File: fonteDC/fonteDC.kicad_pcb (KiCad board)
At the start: 2 copper layers, 13 parts, among them U1 LM7805_TO220

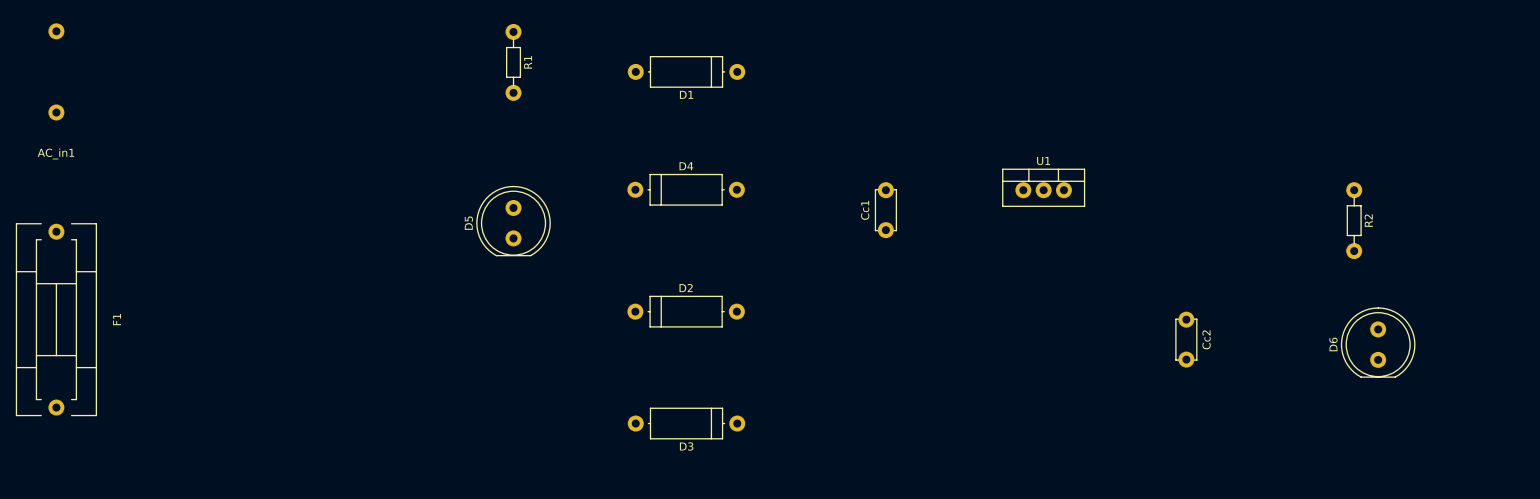
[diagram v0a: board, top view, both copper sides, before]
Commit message: Adicionando capacitores e porta fusível
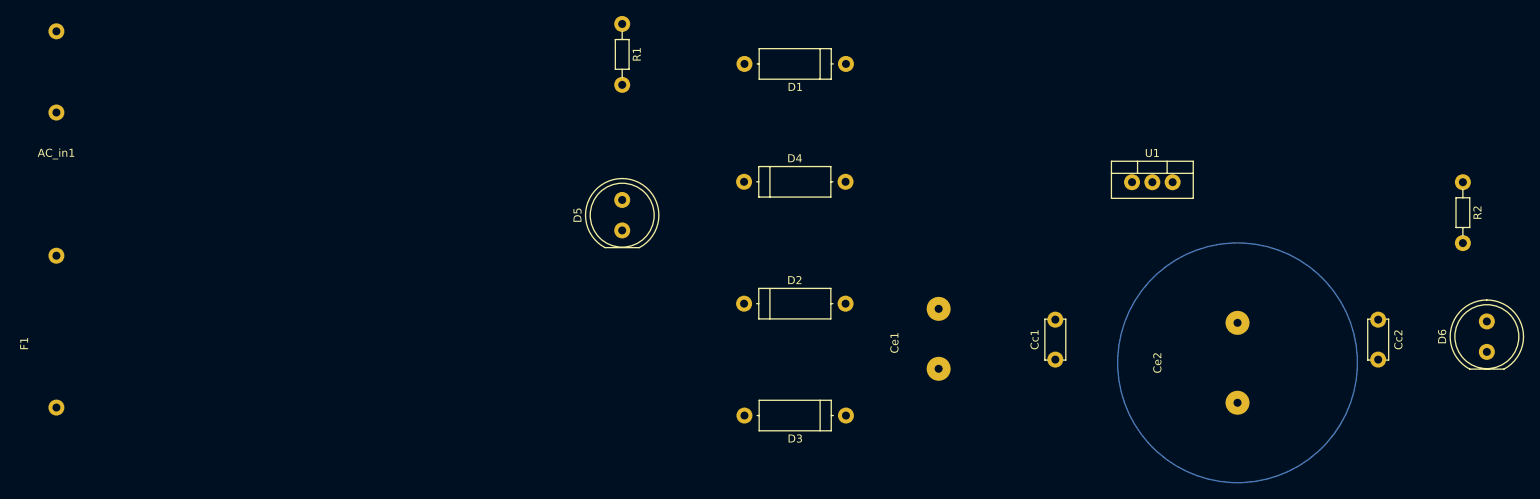
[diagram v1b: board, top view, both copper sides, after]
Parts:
- added Ce1: CP1, fonteDC:CP_elet_7mF, F.Cu at (150.2, 69.4)
- added Ce2: CP1, fonteDC:CP_elet_10mF, F.Cu at (187.6, 66.4)
- F1: footprint fonteDC:Fuseholder5x20_horiz_SemiClosed_Casing10x25mm -> fonteDC:fuseholder
- moved Cc1 26.7 mm to (164.8, 81.0)
- moved Cc2 24.0 mm to (205.2, 76.0)
- moved D6 13.6 mm to (218.8, 79.4)
- moved R2 13.6 mm to (215.8, 58.8)
- moved D1 13.6 mm to (138.6, 44.0)
- moved D2 13.6 mm to (125.8, 74.0)
- moved D3 13.6 mm to (138.6, 88.0)
- moved D4 13.6 mm to (125.8, 58.8)
- moved D5 13.6 mm to (110.6, 64.2)
- moved R1 13.6 mm to (110.6, 39.0)
- moved U1 13.6 mm to (174.4, 58.8)

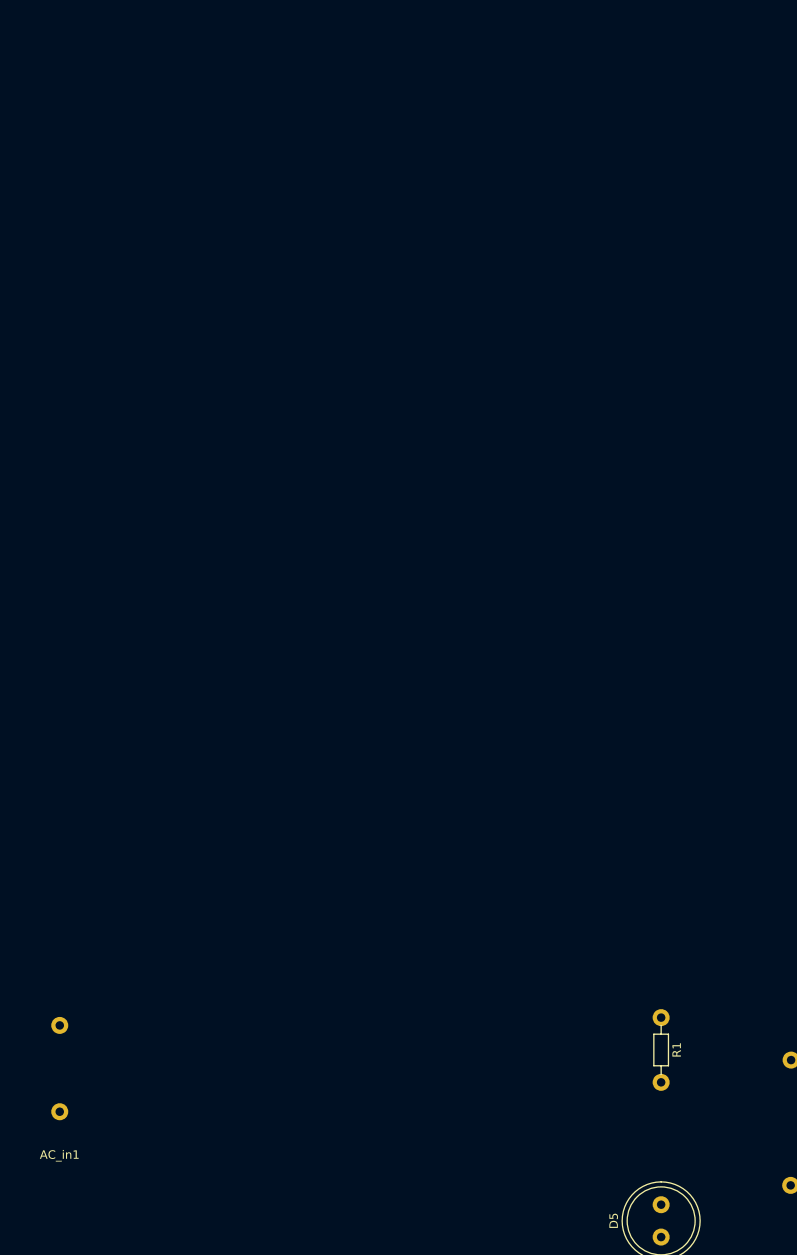
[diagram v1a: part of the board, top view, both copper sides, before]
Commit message: Adicionando footprints da chave seletora de tensão e do transformador
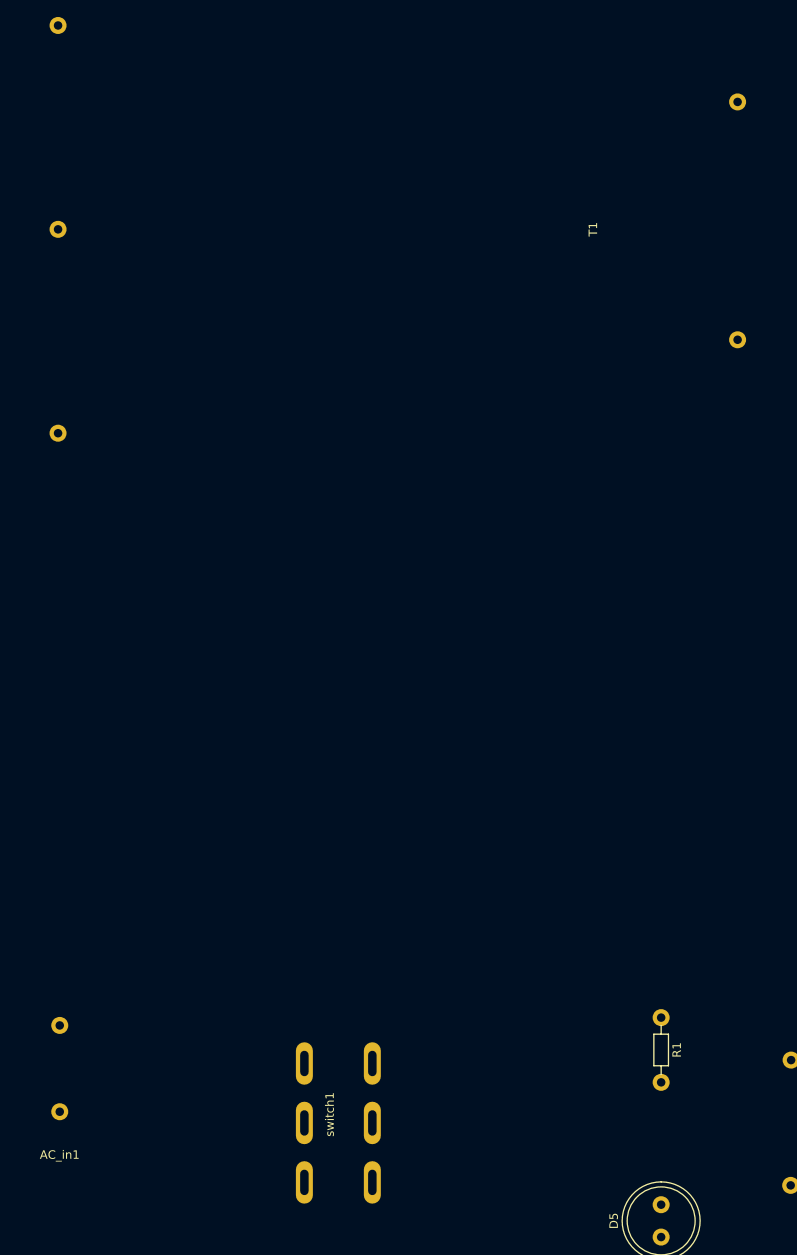
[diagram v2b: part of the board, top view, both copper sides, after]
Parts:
- added T1: Transformer_1P_SS, fonteDC:transformer, F.Cu at (79.6, -9.80)
- added switch1: voltage_switch, fonteDC:swich_110_220, F.Cu at (72.6, 36.4)
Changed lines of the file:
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@@
 (kicad_pcb (version 4) (host pcbnew 4.0.7)
   (general
-    (links 23)
-    (no_connects 23)
+    (links 32)
+    (no_connects 32)
     (area 0 0 0 0)
     (thickness 1.6)
@@
     (tracks 1)
     (zones 0)
-    (modules 15)
-    (nets 9)
+    (modules 17)
+    (nets 11)
   )
   (page A4)
@@
   (net 7 "Net-(AC_in1-Pad2)")
   (net 8 "Net-(AC_in1-Pad1)")
+  (net 9 "Net-(T1-Pad4)")
+  (net 10 "Net-(T1-Pad3)")
   (net_class Default "This is the default net class."
     (clearance 0.2)
@@
     (add_net "Net-(D5-Pad2)")
     (add_net "Net-(D6-Pad2)")
+    (add_net "Net-(T1-Pad3)")
+    (add_net "Net-(T1-Pad4)")
   )
   (module fonteDC:AC_in (layer F.Cu)
@@
       (net 1 GND))
   )
+  (module fonteDC:swich_110_220 (layer F.Cu)
+    (at 72.6 36.4 270)
+    (fp_text reference switch1 (at 14 1 270) (layer F.SilkS)
+      (effects (font (size 1 1) (thickness 0.15)))
+    )
+    (fp_text value voltage_switch (at 14 -2 270) (layer F.Fab)
+      (effects (font (size 1 1) (thickness 0.15)))
+    )
+    (fp_text user VDD110 (at 24 7 270) (layer F.Fab)
+      (effects (font (size 1 1) (thickness 0.15)))
+    )
+    (fp_text user GND110 (at 24 -7 270) (layer F.Fab)
+      (effects (font (size 1 1) (thickness 0.15)))
+    )
+    (fp_text user GND220 (at 6 -7 270) (layer F.Fab)
+      (effects (font (size 1 1) (thickness 0.15)))
+    )
+    (fp_text user VDD220 (at 6 7 270) (layer F.Fab)
+      (effects (font (size 1 1) (thickness 0.15)))
+    )
+    (fp_text user GND (at 15 -7 270) (layer F.Fab)
+      (effects (font (size 1 1) (thickness 0.15)))
+    )
+    (fp_text user VDD (at 15 7 270) (layer F.Fab)
+      (effects (font (size 1 1) (thickness 0.15)))
+    )
+    (fp_line (start 0 -8) (end 0 8) (layer F.Fab) (width 0.15))
+    (fp_line (start 30 -8) (end 30 8) (layer F.Fab) (width 0.15))
+    (fp_line (start 0 8) (end 30 8) (layer F.Fab) (width 0.15))
+    (fp_line (start 0 -8) (end 30 -8) (layer F.Fab) (width 0.15))
+    (pad 6 thru_hole oval (at 22 -4 270) (size 5 2) (drill oval 3 1) (layers *.Cu *.Mask)
+      (net 1 GND))
+    (pad 5 thru_hole oval (at 22 4 270) (size 5 2) (drill oval 3 1) (layers *.Cu *.Mask)
+      (net 9 "Net-(T1-Pad4)"))
+    (pad 4 thru_hole oval (at 8 -4 270) (size 5 2) (drill oval 3 1) (layers *.Cu *.Mask)
+      (net 1 GND))
+    (pad 3 thru_hole oval (at 8 4 270) (size 5 2) (drill oval 3 1) (layers *.Cu *.Mask)
+      (net 10 "Net-(T1-Pad3)"))
+    (pad 2 thru_hole oval (at 15 -4 270) (size 5 2) (drill oval 3 1) (layers *.Cu *.Mask)
+      (net 1 GND))
+    (pad 1 thru_hole oval (at 15 4 270) (size 5 2) (drill oval 3 1) (layers *.Cu *.Mask)
+      (net 8 "Net-(AC_in1-Pad1)"))
+  )
+  (module fonteDC:transformer (layer F.Cu)
+    (at 79.6 -9.8 90)
+    (fp_text reference T1 (at 44 23 90) (layer F.SilkS)
+      (effects (font (size 1 1) (thickness 0.15)))
+    )
+    (fp_text value Transformer_1P_SS (at 44 -22 90) (layer F.Fab)
+      (effects (font (size 1 1) (thickness 0.15)))
+    )
+    (fp_line (start 1 -41) (end 83 -41) (layer F.CrtYd) (width 0.15))
+    (fp_line (start 83 41) (end 0.5 41) (layer F.CrtYd) (width 0.15))
+    (fp_line (start 83 41) (end 83 -41) (layer F.CrtYd) (width 0.15))
+    (fp_line (start 0 -41) (end 0 41) (layer F.CrtYd) (width 0.15))
+    (fp_line (start 0 41) (end 0.5 41) (layer F.CrtYd) (width 0.15))
+    (fp_line (start 1 -41) (end 0 -41) (layer F.CrtYd) (width 0.15))
+    (fp_line (start 73 -2.5) (end 73 2.5) (layer F.Fab) (width 0.15))
+    (fp_line (start 81 -2.5) (end 73 -2.5) (layer F.Fab) (width 0.15))
+    (fp_line (start 81 -2.5) (end 81 2.5) (layer F.Fab) (width 0.15))
+    (fp_line (start 81 2.5) (end 73 2.5) (layer F.Fab) (width 0.15))
+    (fp_line (start 10.5 2.5) (end 10.5 -2.5) (layer F.Fab) (width 0.15))
+    (fp_line (start 2.5 -2.5) (end 10.5 -2.5) (layer F.Fab) (width 0.15))
+    (fp_line (start 2.5 -2.5) (end 2.5 2.5) (layer F.Fab) (width 0.15))
+    (fp_line (start 2.5 2.5) (end 10.5 2.5) (layer F.Fab) (width 0.15))
+    (fp_text user GND (at 68.5 -35.5 90) (layer F.Fab)
+      (effects (font (size 3 3) (thickness 0.15)))
+    )
+    (fp_text user 110 (at 44 -35.5 90) (layer F.Fab)
+      (effects (font (size 3 3) (thickness 0.15)))
+    )
+    (fp_text user 220 (at 20 -35.5 90) (layer F.Fab)
+      (effects (font (size 3 3) (thickness 0.15)))
+    )
+    (fp_line (start 57 35) (end 61 35) (layer F.Fab) (width 0.15))
+    (fp_line (start 31 37) (end 31 33) (layer F.Fab) (width 0.15))
+    (fp_line (start 29 35) (end 33 35) (layer F.Fab) (width 0.15))
+    (fp_line (start 0 25) (end 0 -25) (layer F.Fab) (width 0.15))
+    (fp_line (start 83 -25) (end 83 25) (layer F.Fab) (width 0.15))
+    (fp_line (start 0 25) (end 83 25) (layer F.Fab) (width 0.15))
+    (fp_line (start 0 -25) (end 83 -25) (layer F.Fab) (width 0.15))
+    (pad 5 thru_hole circle (at 68 -40 90) (size 2 2) (drill 1) (layers *.Cu *.Mask)
+      (net 1 GND))
+    (pad 4 thru_hole circle (at 44 -40 90) (size 2 2) (drill 1) (layers *.Cu *.Mask)
+      (net 9 "Net-(T1-Pad4)"))
+    (pad 3 thru_hole circle (at 20 -40 90) (size 2 2) (drill 1) (layers *.Cu *.Mask)
+      (net 10 "Net-(T1-Pad3)"))
+    (pad 1 thru_hole circle (at 59 40 90) (size 2 2) (drill 1) (layers *.Cu *.Mask)
+      (net 4 "Net-(D2-Pad1)"))
+    (pad 2 thru_hole circle (at 31 40 90) (size 2 2) (drill 1) (layers *.Cu *.Mask)
+      (net 3 "Net-(D1-Pad2)"))
+  )
   (gr_line (start 230 30) (end 230 130) (angle 90) (layer F.Fab) (width 0.2))

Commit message: almost done.
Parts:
- added J1: Conn_01x02, fonteDC:AC_in, F.Cu at (42.0, 163.0)
- D5, D6: footprint fonteDC:LED_D8.0mm -> Diodes_THT:D_T-1_P12.70mm_Horizontal
- moved R2 200.2 mm to (31.7, 137.3)
- moved D6 186.8 mm to (46.9, 152.6), turned to 180 degrees
- moved Cc2 182.0 mm to (31.7, 131.0), turned to 0 degrees
- moved Ce2 171.0 mm to (22.0, 109.0), turned to 0 degrees
- moved T1 124.9 mm to (121.0, 108.0)
- moved U1 119.2 mm to (113.0, 161.0), turned to 180 degrees
- moved D2 95.6 mm to (192.5, 142.5), turned to 180 degrees
- moved D1 81.5 mm to (179.5, 114.5), turned to 0 degrees
- moved D4 79.7 mm to (192.5, 102.5), turned to 180 degrees
- moved Ce1 67.1 mm to (161.5, 135.5), turned to 90 degrees
- moved R1 66.6 mm to (166.0, 76.0), turned to 90 degrees
- moved D3 59.0 mm to (179.5, 130.5), turned to 0 degrees
- moved D5 57.4 mm to (166.0, 49.0), turned to 270 degrees
- moved Cc1 52.8 mm to (145.0, 130.0)
- moved switch1 11.5 mm to (62.0, 32.0)
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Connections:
- Cc1 pad 1: GND -> Net-(Cc1-Pad1)
- Cc1 pad 2: GND -> Net-(Cc1-Pad2)
- Cc2 pad 2: GND -> Net-(Cc1-Pad2)
- Ce1 pad 1: GND -> Net-(Cc1-Pad1)
- Ce1 pad 2: GND -> Net-(Cc1-Pad2)
- Ce2 pad 2: GND -> Net-(Cc1-Pad2)
- D1 pad 1: GND -> Net-(Cc1-Pad1)
- D2 pad 2: GND -> Net-(Cc1-Pad2)
- D3 pad 1: GND -> Net-(Cc1-Pad1)
- D4 pad 2: GND -> Net-(Cc1-Pad2)
- D6 pad 1: GND -> Net-(Cc1-Pad2)
- F1 pad 2: GND -> Net-(F1-Pad2)
- T1 pad 5: GND -> Net-(T1-Pad5)
- U1 pad 1: GND -> Net-(Cc1-Pad1)
- U1 pad 2: GND -> Net-(Cc1-Pad2)
- switch1 pad 2: GND -> Net-(F1-Pad2)
- switch1 pad 4: GND -> Net-(T1-Pad5)
- switch1 pad 6: GND -> Net-(T1-Pad5)
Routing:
- net Net-(Cc1-Pad2): track 0.00 -> 415.2 mm
- net Net-(Cc2-Pad1): track 0.00 -> 192.0 mm
- net Net-(T1-Pad3): track 0.00 -> 139.1 mm
- net Net-(F1-Pad2): track 0.00 -> 133.4 mm
- net Net-(D2-Pad1): track 0.00 -> 122.5 mm
- net Net-(Cc1-Pad1): track 0.00 -> 101.8 mm
- net Net-(D1-Pad2): track 0.00 -> 64.4 mm
- net Net-(T1-Pad4): track 0.00 -> 51.5 mm
- net Net-(T1-Pad5): track 0.00 -> 44.0 mm, vias 0 -> 2
- net Net-(AC_in1-Pad1): track 0.00 -> 15.9 mm
- net Net-(AC_in1-Pad2): track 0.00 -> 14.0 mm
- net Net-(D6-Pad2): track 0.00 -> 8.67 mm
- net Net-(D5-Pad2): track 0.00 -> 6.68 mm
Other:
- board outline added: 184 x 150 mm
- net class Default: clearance 0.2 -> 1; via_dia 0.6 -> 2; via_drill 0.4 -> 1
- rule trace_clearance: 0.2 -> 1
- rule via_min_size: 0.4 -> 1

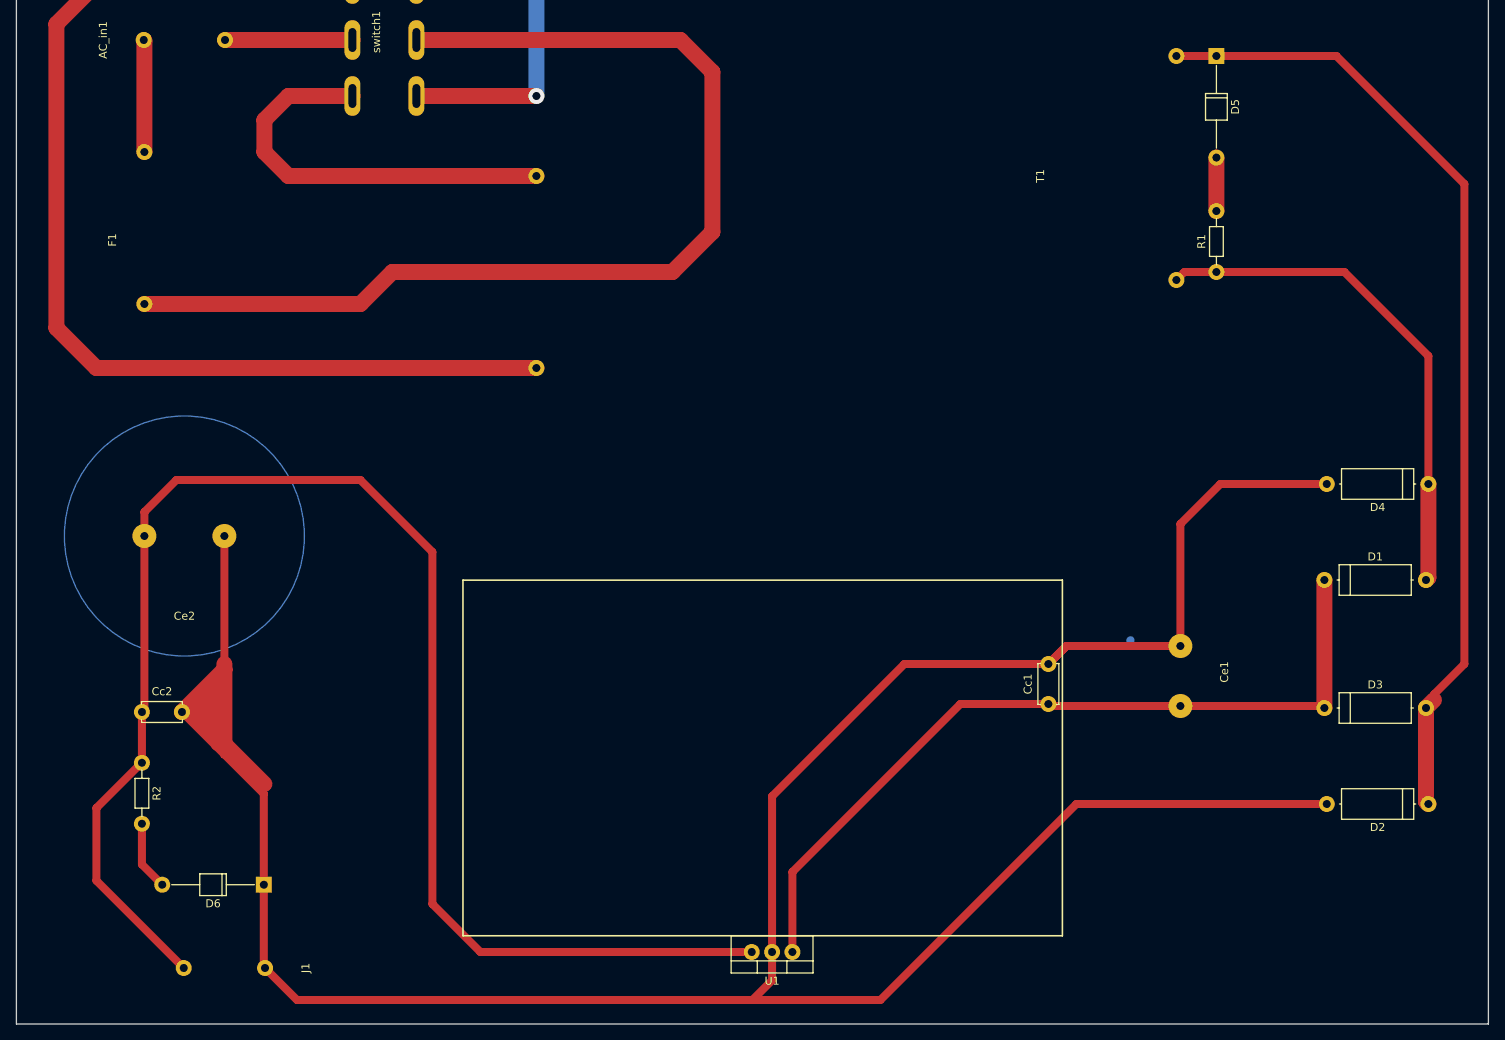
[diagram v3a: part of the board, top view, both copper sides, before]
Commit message: Reforçando algumas conexões
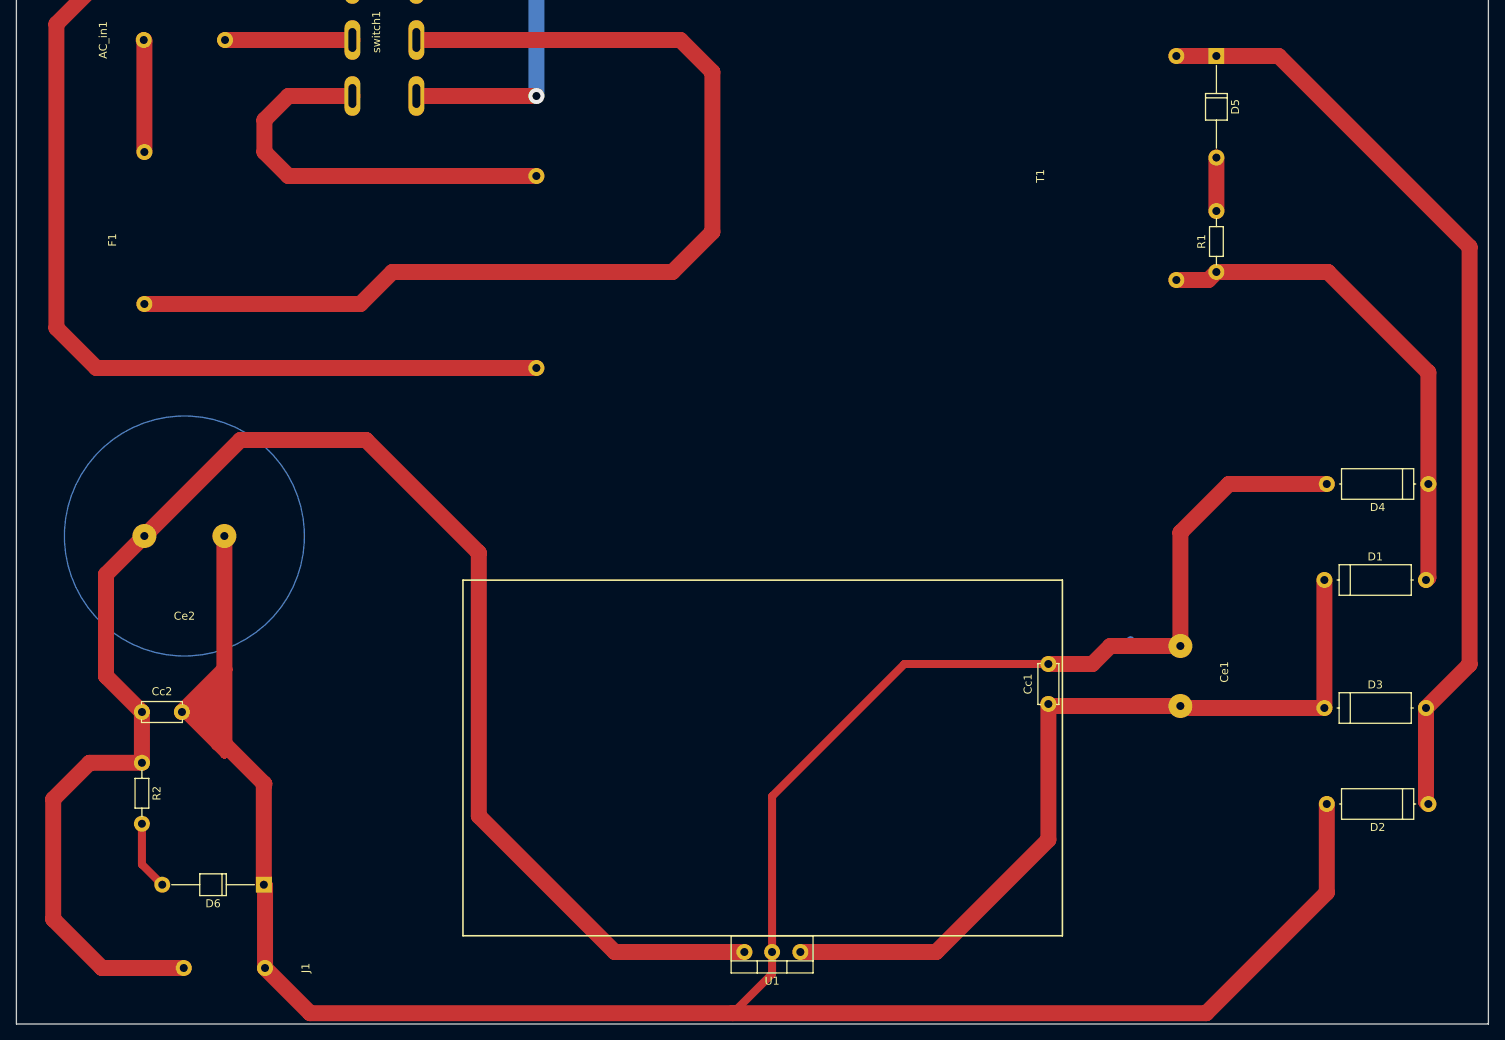
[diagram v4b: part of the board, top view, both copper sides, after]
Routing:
- net Net-(Cc2-Pad1): track 192.0 -> 205.5 mm
- net Net-(Cc1-Pad1): track 101.8 -> 105.5 mm
- net Net-(D2-Pad1): track 122.5 -> 120.8 mm
- net Net-(Cc1-Pad2): track 415.2 -> 416.6 mm
- net Net-(D1-Pad2): track 64.4 -> 63.2 mm
